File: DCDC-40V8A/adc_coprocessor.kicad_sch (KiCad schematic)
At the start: 31 parts, among them Q10 2N7002, Q11 2N7002, Q12 2N7002, Q13 2N7002, Q14 2N7002, Q15 2N7002, Q16 2N7002, Q17 2N7002, Q18 2N7002, Q19 2N7002, Q20 2N7002, Q5 2N7002, Q6 2N7002, Q7 2N7002, Q8 2N7002, Q9 2N7002, U10 CD4051B, U11 CD4051B, U12 CD4051B, U6 74HC595, U7 74HC595, U8 74HC595, U9 CD4051B

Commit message: wip
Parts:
- added C39, C40, C41, C42, C43: 100n, Capacitor_SMD:C_0603_1608Metric, symbol Device:C
- added Q21, Q22: 2N7002, Package_TO_SOT_SMD:SOT-23, symbol Transistor_FET:2N7002
- added R20: 4.7k, Resistor_SMD:R_0603_1608Metric, symbol Device:R
- added U13: CD4051B, Package_SO:SOIC-16_3.9x9.9mm_P1.27mm, symbol Analog_Switch:CD4051B
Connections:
- net +3V3: now also C39.1, C40.1, C41.1, C42.1, C43.1, U13.16 (VDD)
- net ADC_IN: now also U13.3 (X)
- net ADC_SEL_3: now also U13.11 (A)
- net ADC_SEL_4: now also U13.10 (B)
- net CHAN_A_EN: now also U6.15 (QA); no longer U6.2 (QC)
- net CHAN_B_EN: now also U6.1 (QB); no longer U6.3 (QD)
- net FAN_EN: now also U6.2 (QC); no longer U6.4 (QE)
- net GND: now also C39.2, C40.2, C41.2, C42.2, C43.2, Q21.2 (S), Q22.2 (S), U13.1 (X4), U13.2 (X6), U13.4 (X7), U13.5 (X5), U13.6 (INH), U13.7 (VEE), U13.8 (VSS), U13.9 (C)
- net PWR_IN_EN: now also U5.11 (PA17/A9), Q21.1 (G); no longer U6.15 (QA)
- net PWR_OUT_EN: now also U5.10 (PA16/A8), Q22.1 (G); no longer U6.1 (QB)
- net ADC_A: now reaches U9.3 (X)
- net ADC_A: now also U13.13 (X0)
- net at U5.12 (PA18/A7): now also R20.2
- net ADC_B: now reaches U10.3 (X)
- net ADC_B: now also U13.14 (X1)
- net ADC_D: now reaches U12.3 (X)
- net ADC_D: now also U13.12 (X3)
- net USB_5V_EN: now reaches U6.5 (QF)
- net TEMP_7_ADC: now reaches U11.2 (X6)
- net ADC_C: now reaches U11.3 (X)
- net ADC_C: now also U13.15 (X2)
- net TEMP_8_ADC: now reaches U11.4 (X7)
- new net BAT_5V_EN: U6.4 (QE)
- new net MAIN_5V_EN: U6.3 (QD)
- new net PWR_5V_EN: Q21.3 (D), Q22.3 (D), R20.1
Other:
- moved on the sheet: C33, C34, C35, Q10, Q11, Q12, Q5, Q6, Q7, Q8, Q9, R17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

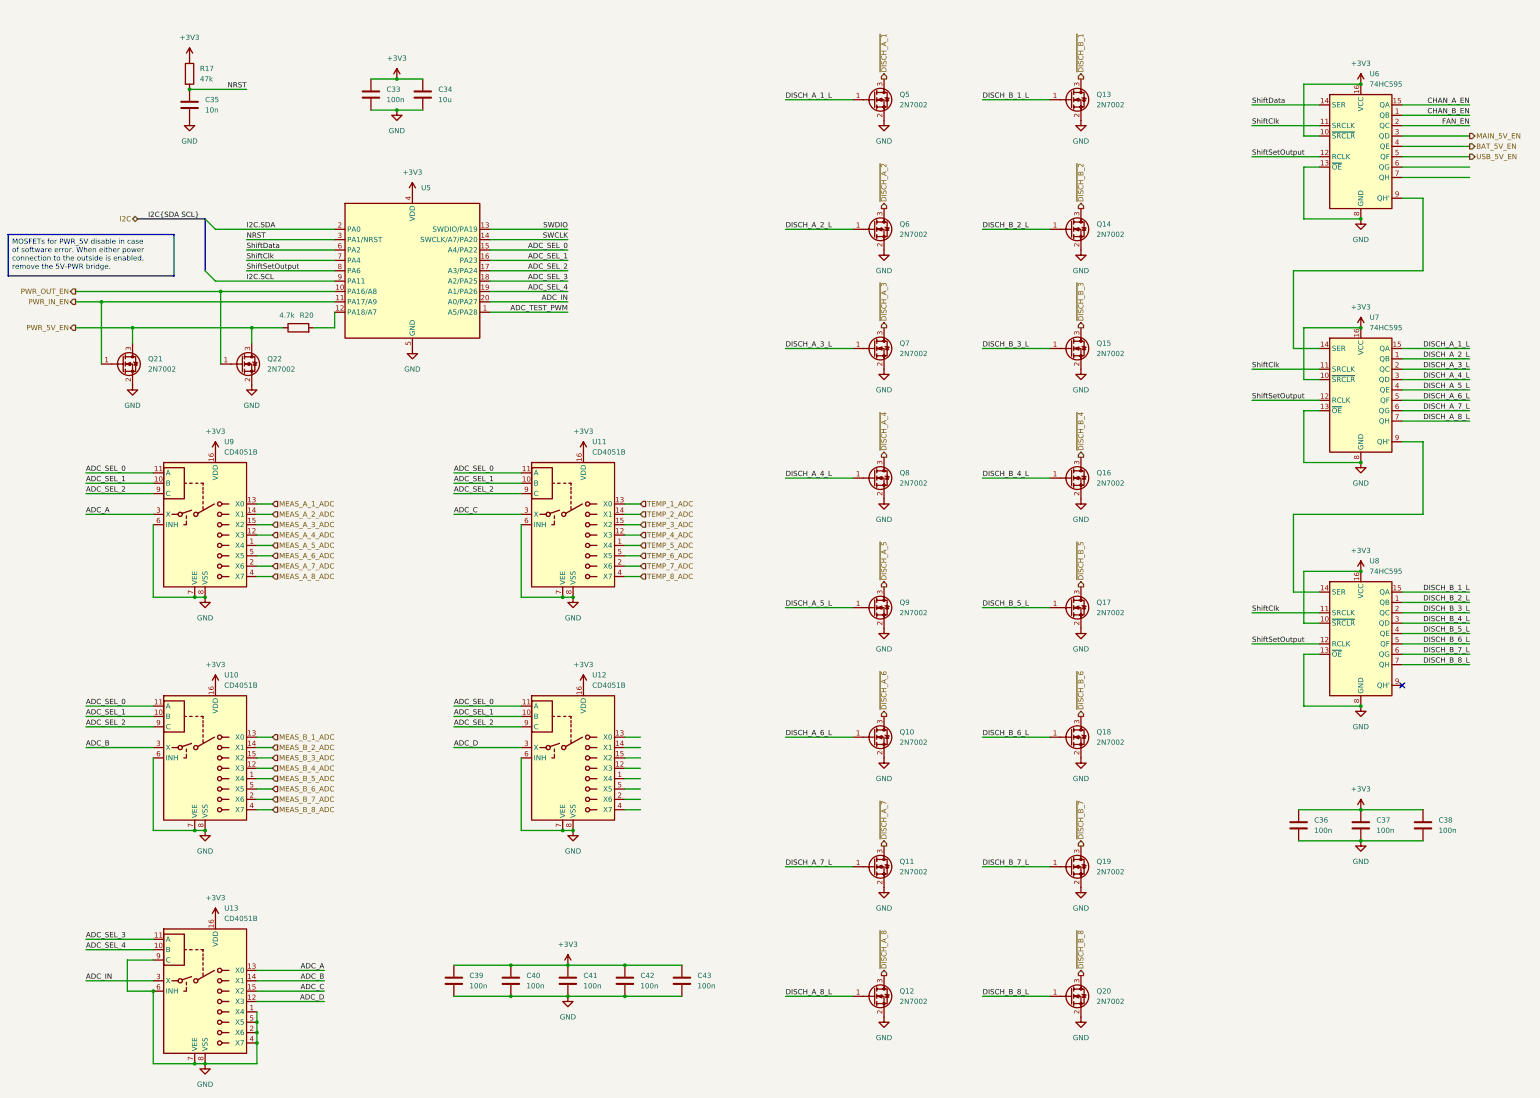
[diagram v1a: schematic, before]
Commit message: move adc MUX and discharge to new sheet
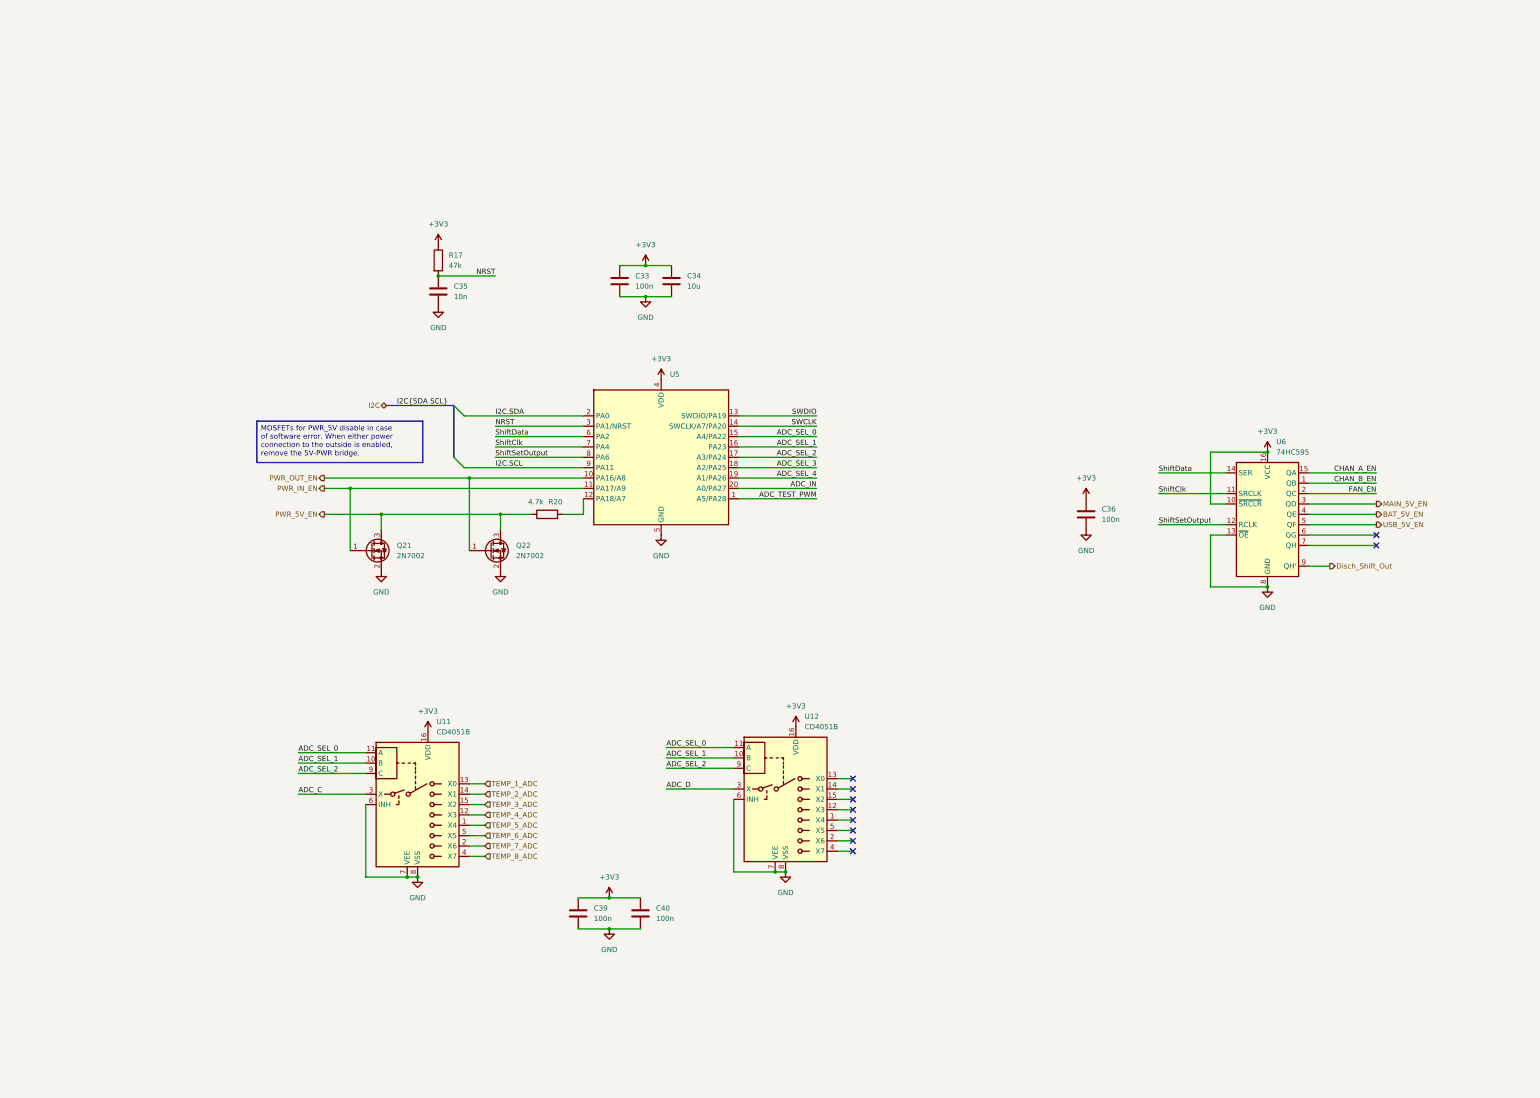
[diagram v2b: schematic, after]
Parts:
- removed C37, C38, C41, C42, C43: 100n, Capacitor_SMD:C_0603_1608Metric, symbol Device:C
- removed Q10, Q11, Q12, Q13, Q14, Q15, Q16, Q17, Q18, Q19, Q20, Q5, Q6, Q7, Q8, Q9: 2N7002, Package_TO_SOT_SMD:SOT-23, symbol Transistor_FET:2N7002
- removed U10, U13, U9: CD4051B, Package_SO:SOIC-16_3.9x9.9mm_P1.27mm, symbol Analog_Switch:CD4051B
- removed U7, U8: 74HC595, Package_SO:SOIC-16_3.9x9.9mm_P1.27mm, symbol 74xx:74HC595
- U5: value ~ -> (none)
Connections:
- net Disch_Shift_Out: now reaches U6.9 (QH')
- no-connect marks 1 -> 10
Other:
- moved on the sheet: C33, C34, C35, C39, C40, Q21, Q22, R17, R20, U11, U12, U5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

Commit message: added discharge circuitry and help texts
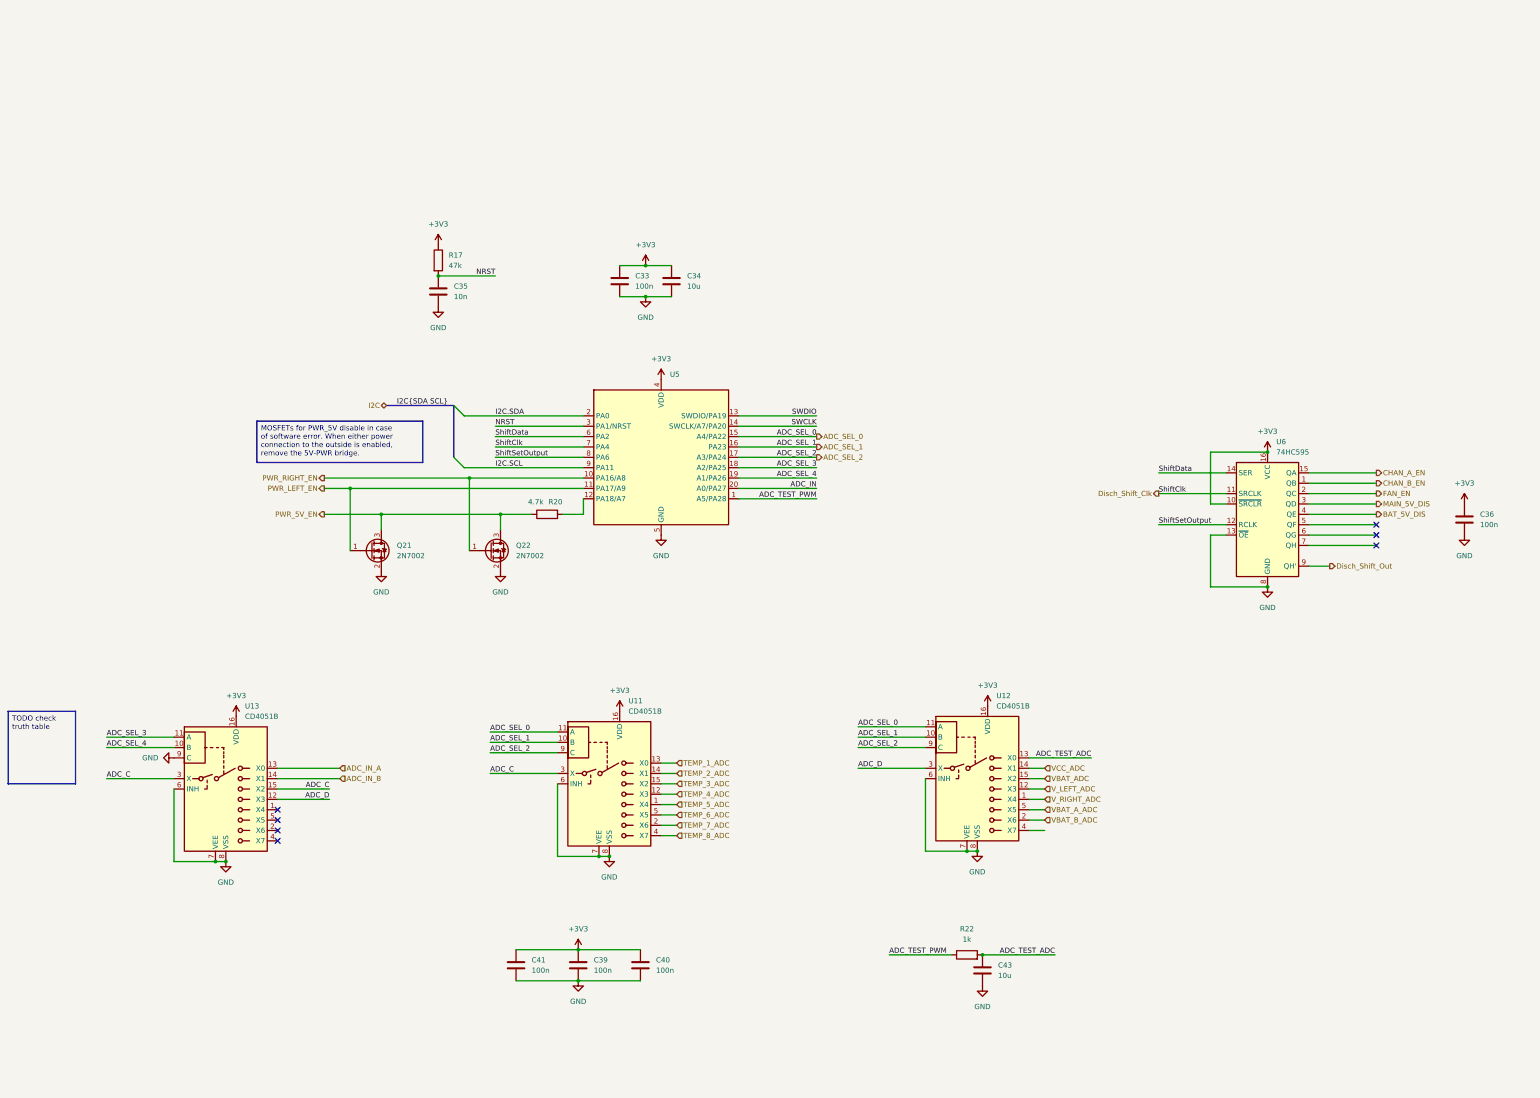
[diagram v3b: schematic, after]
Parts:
- added C41: 100n, Capacitor_SMD:C_0603_1608Metric, symbol Device:C
- added C43: 10u, Capacitor_SMD:C_0603_1608Metric, symbol Device:C
- added R22: 1k, Capacitor_SMD:C_0603_1608Metric, symbol Device:R
- added U13: CD4051B, Package_SO:SOIC-16_3.9x9.9mm_P1.27mm, symbol Analog_Switch:CD4051B
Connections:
- net +3V3: now also C41.1, U13.16 (VDD)
- net ADC_C: now also U13.15 (X2), U13.3 (X)
- net ADC_D: now also U13.12 (X3)
- net ADC_SEL_3: now also U13.11 (A)
- net ADC_SEL_4: now also U13.10 (B)
- net ADC_TEST_PWM: now also R22.1
- net GND: now also C41.2, C43.2, U13.6 (INH), U13.7 (VEE), U13.8 (VSS), U13.9 (C)
- net V_RIGHT_ADC: now reaches U12.1 (X4)
- net V_LEFT_ADC: now reaches U12.12 (X3)
- net ADC_TEST_ADC: now reaches U12.13 (X0)
- net ADC_TEST_ADC: now also C43.1, R22.2
- net VCC_ADC: now reaches U12.14 (X1)
- net VBAT_ADC: now reaches U12.15 (X2)
- net VBAT_B_ADC: now reaches U12.2 (X6)
- net VBAT_A_ADC: now reaches U12.5 (X5)
- net BAT_5V_EN renamed BAT_5V_DIS
- net MAIN_5V_EN renamed MAIN_5V_DIS
- net PWR_IN_EN renamed PWR_LEFT_EN
- net PWR_OUT_EN renamed PWR_RIGHT_EN
- net ShiftClk renamed Disch_Shift_Clk
- net USB_5V_EN: no longer names the net of U6.5 (QF)
- new net ADC_IN_A: U13.13 (X0)
- new net ADC_IN_B: U13.14 (X1)
- no-connect marks 10 -> 7
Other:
- moved on the sheet: C36, C39, C40, U11, U12

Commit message: wip
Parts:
- removed C41: 100n, Capacitor_SMD:C_0603_1608Metric, symbol Device:C
- removed Q21: 2N7002, Package_TO_SOT_SMD:SOT-23, symbol Transistor_FET:2N7002
- removed U13: CD4051B, Package_SO:SOIC-16_3.9x9.9mm_P1.27mm, symbol Analog_Switch:CD4051B
- added C46: 100n, Capacitor_SMD:C_0402_1005Metric, symbol Device:C
- added Q44: 2N7002, Package_TO_SOT_SMD:SOT-23, symbol Transistor_FET:2N7002
- added R160, R163: 4.7k, Resistor_SMD:R_0402_1005Metric, symbol Device:R
- added R161, R162: 1k, Resistor_SMD:R_0402_1005Metric, symbol Device:R
- added R21: 220k, Resistor_SMD:R_0402_1005Metric, symbol Device:R
- added R23: 10k, Resistor_SMD:R_0402_1005Metric, symbol Device:R
- added R92, R93, R94: 47k, Resistor_SMD:R_0603_1608Metric, symbol Device:R
- added R95: 10k, Resistor_SMD:R_0603_1608Metric, symbol Device:R
- added U20: Opamp_Dual, Package_SO:TSSOP-8_3x3mm_P0.65mm, symbol Device:Opamp_Dual
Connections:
- net ADC_IN is gone; now on net ADC_C: U5.20 (A0/PA27)
- net PWR_LEFT_EN is gone; now on net ADC_TEST_PWM: U5.11 (PA17/A9)
- net V_LEFT_ADC is gone; now on net VBAT_A_ADC: U12.12 (X3)
- net V_RIGHT_ADC is gone; now on net VBAT_B_ADC: U12.1 (X4)
- net +3V3: now also C46.1, U20.8 (V+)
- net ADC_D: now also U5.1 (A5/PA28)
- net ADC_IN_A: now also U20.3 (+)
- net ADC_IN_B: now also U20.5 (+)
- net ADC_TEST_PWM: no longer U5.1 (A5/PA28)
- net FAN_EN: now also U5.10 (PA16/A8); no longer U6.2 (QC)
- net GND: now also C46.2, Q44.2 (S), R161.1, R162.1, R23.2, R93.2, R95.2, U20.4 (V-)
- net PWR_5V_EN: now also R20.2, Q44.3 (D); no longer R20.1
- net VBAT_A_ADC: no longer U12.5 (X5)
- net VBAT_B_ADC: no longer U12.2 (X6)
- net at U5.12 (PA18/A7): no longer R20.2
- net V_HI_DRV_ADC: now reaches U12.4 (X7)
- net V_HI_DRV_ADC: now also R21.2, R23.1
- net PWR_RAIL_EN: now reaches U6.5 (QF)
- net PWR_RAIL_EN: now also Q22.1 (G)
- net PWR_XT60IN_EN: now reaches U6.6 (QG)
- net PWR_XT60IN_EN: now also Q44.1 (G)
- net at U6.7 (QH): now also R20.1
- net ADC_SEL_3 renamed CP_PWM
- net ADC_SEL_4: no longer names the net of U5.19 (A1/PA26)
- net BAT_5V_DIS renamed BAT_DCDC_DIS
- net MAIN_5V_DIS renamed 5V_DCDC_DIS
- removed net PWR_RIGHT_EN: Q22.1 (G), U5.10 (PA16/A8)
- net VBAT_ADC renamed V_XT60IN_ADC
- net VCC_ADC renamed V_RAIL_ADC
- new net: R160.1, R161.2, U20.2 (-)
- new net: R162.2, R163.1, U20.6 (-)
- new net +12V: R94.1
- new net +5V: R92.1
- new net 12V_ADC: R94.2, R95.1, U12.2 (X6)
- new net 5V_ADC: R92.2, R93.1, U12.5 (X5)
- new net ADC_A: R160.2, U20.1
- new net ADC_B: R163.2, U20.7
- new net V_HI_DRV: R21.1
- no-connect marks 7 -> 2
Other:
- moved on the sheet: C33, C34, C35, C36, C39, C40, C43, R17, R22, U11, U12, U5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

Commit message: wip before CP deletion
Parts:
- removed Q44: 2N7002, Package_TO_SOT_SMD:SOT-23, symbol Transistor_FET:2N7002
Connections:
- net CP_PWM: no longer names the net of U5.18 (A2/PA25)
- net PWR_RAIL_EN: no longer names the net of U6.5 (QF)
- net PWR_RAIL_EN: no longer Q22.1 (G)
- net PWR_XT60IN_EN renamed PWR_EXT_EN
- net PWR_EXT_EN: now also Q22.1 (G)
- net V_RAIL_ADC renamed V_EXT_ADC
- net V_XT60IN_ADC: no longer names the net of U12.15 (X2)
- no-connect marks 2 -> 6
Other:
- moved on the sheet: Q22

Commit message: renumbering
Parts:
- renumbered C46 to C37, C39 to C38, C40 to C39, C43 to C40, Q22 to Q13, R17 to R28, R20 to R29, R160 to R30, R163 to R31, R92 to R32, R94 to R33, R21 to R34, R161 to R35, R162 to R36, R93 to R37, R95 to R38, R23 to R39, R22 to R40, U6 to U5, U5 to U6, U20 to U7, U12 to U8, U11 to U9

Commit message: schematics done?
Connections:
- net 12V_EN: now reaches U5.5 (QF)
- no-connect marks 6 -> 5
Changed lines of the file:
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@@
-	)
-	(no_connect
-		(at 269.24 102.87)
 	)
 	(no_connect
@@
 	(wire
 		(pts
+			(xy 269.24 102.87) (xy 285.75 102.87)
+		)
+		(stroke
+			(width 0)
+			(type default)
+		)
+	)
+	(wire
+		(pts
 			(xy 210.82 232.41) (xy 227.33 232.41)
 		)
@@
 		(effects
 			(font
+				(size 1.27 1.27)
+			)
+			(justify left)
+		)
+	)
+	(hierarchical_label "12V_EN"
+		(shape output)
+		(at 285.75 102.87 0)
+		(effects
+			(font
